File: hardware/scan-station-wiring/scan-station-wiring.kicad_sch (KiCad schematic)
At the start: 57 parts, among them J10 Buttons/Encoder, J11 GPIO Expansion, J1A CYD Expansion (SPI2), J1B CYD UART (PWR+HS), J2 NFC Antenna A, J3 RGB LED Header, J4 NFC Antenna B, J5 USB-C Power, J6 Load Cell, J7 CAN Bus, J8 I2C1 Expansion, J9 TOF Sensor (I2C1), Q1 TVDD_SW_A, Q2 TVDD_SW_B, Q3 BSS138 (SDA), Q4 BSS138 (SCL), U1 ESP32-S3-DevKitC-1, U2 ADS1220IPWR, U3 AHT20, U4 PN5180A0HN, U5 AS7341-DLGM, U6 AMS1117-3.3, U7 SN65HVD230DR, U8 AMS1117-1.8, Y1 27.12MHz

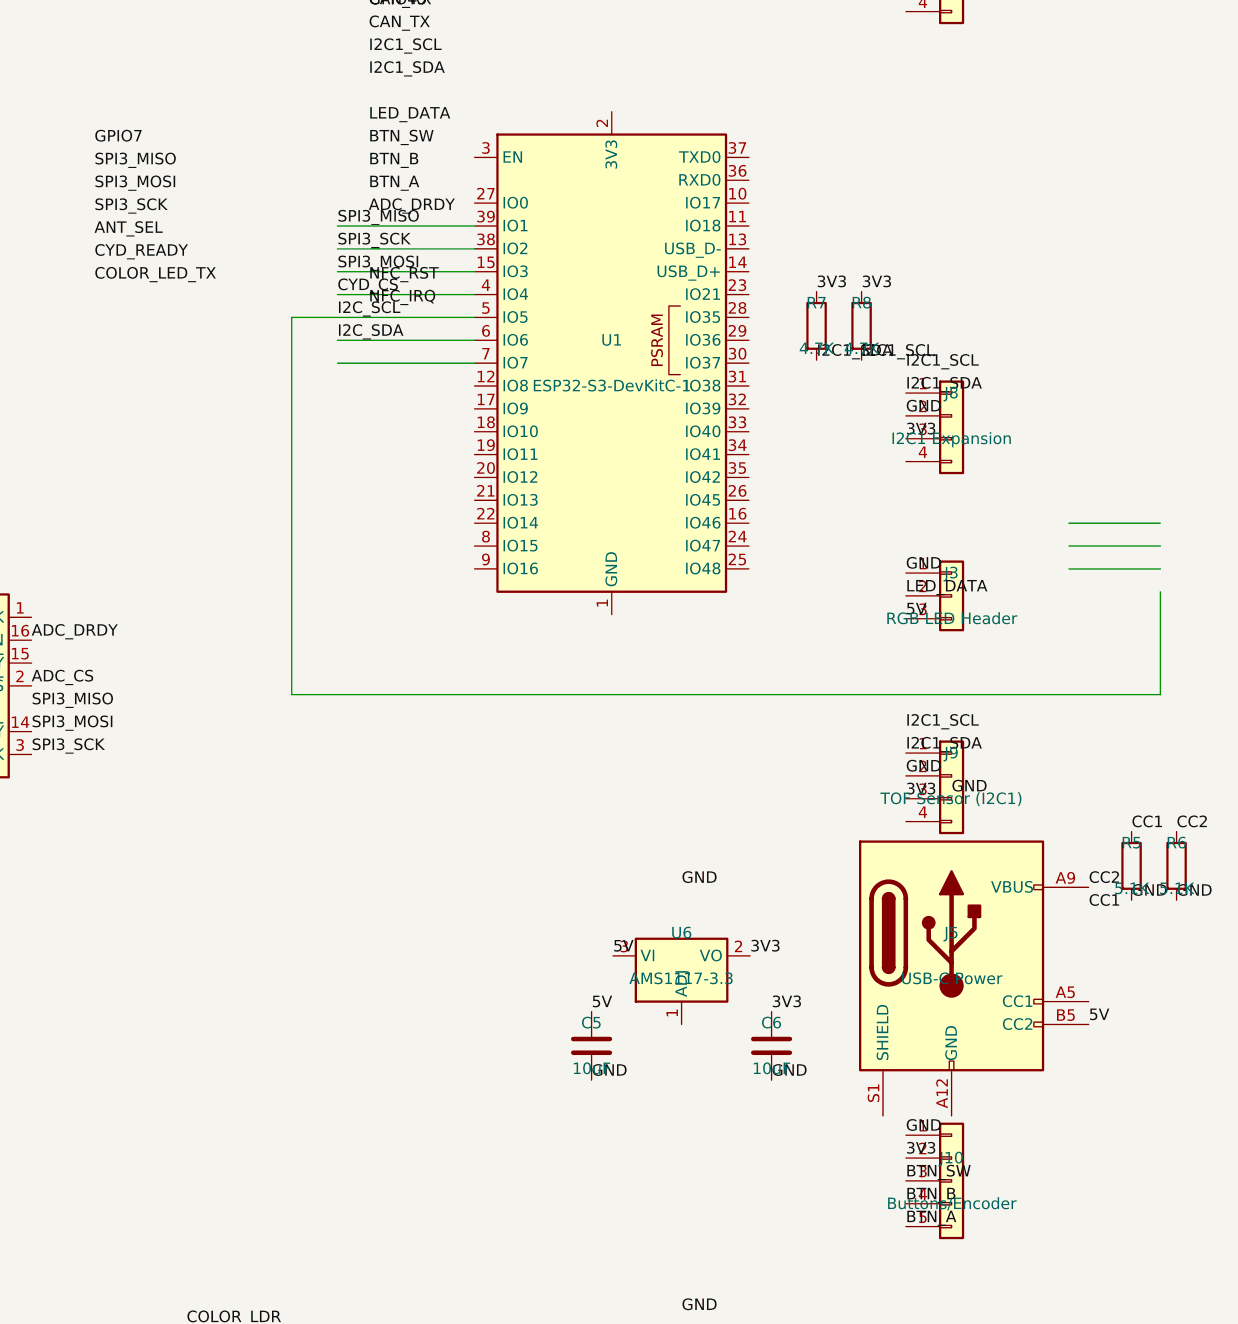
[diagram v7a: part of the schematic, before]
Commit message: feat: switch from DevKitC to bare ESP32-S3-WROOM-1 module
Eliminates redundant USB, regulator, and buttons from DevKitC.
Adds required support circuitry for bare module:

- EN circuit: 10K pull-up + 1uF cap + reset button (SW1)
- Boot button (SW2): GPIO0 + 10K pull-up
- Native USB: 22R series resistors on D+/D-, upgraded J5 to
  USB-C 2.0 14P receptacle (was power-only 6P)
- Module decoupling: 10uF + 100nF on 3V3 input
- Saves ~$5/board vs DevKitC, smaller PCB footprint

Co-Authored-By: Claude Opus 4.6 (1M context) <noreply@anthropic.com>
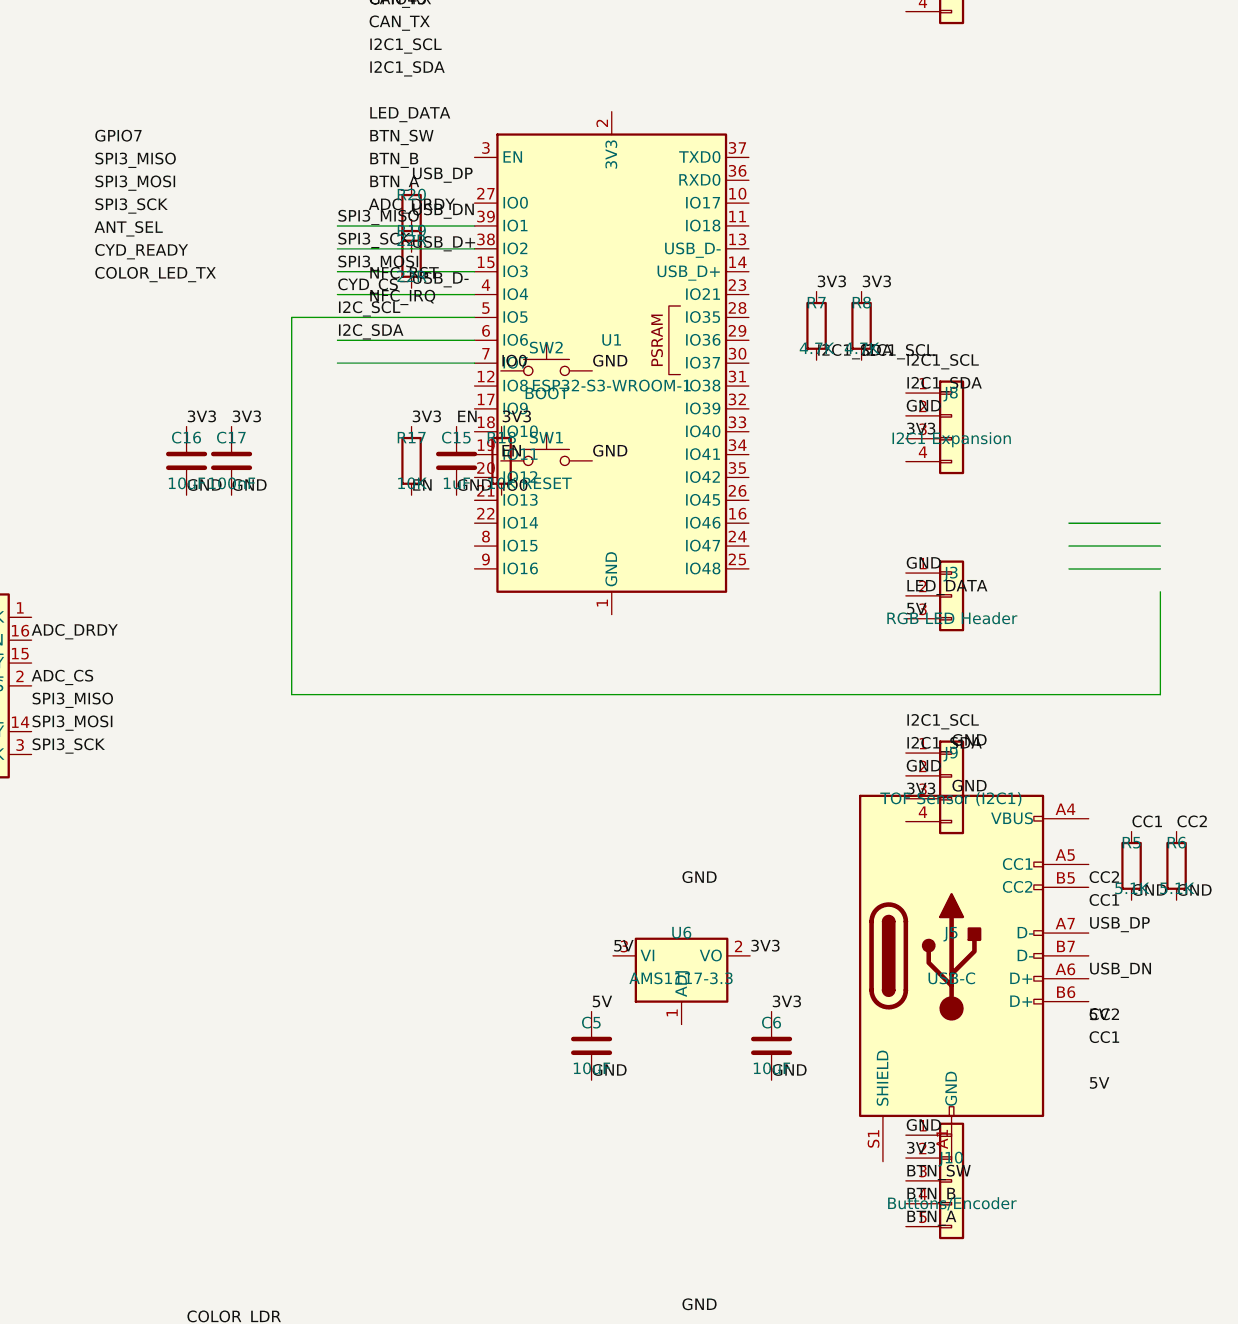
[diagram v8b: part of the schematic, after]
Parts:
- removed J5: USB-C Power, symbol Connector:USB_C_Receptacle_PowerOnly_6P
- added C15: 1uF, symbol Device:C
- added C16: 10uF, symbol Device:C
- added C17: 100nF, symbol Device:C
- added J5: USB-C, symbol Connector:USB_C_Receptacle_USB2.0_14P
- added R17, R18: 10K, symbol Device:R
- added R19, R20: 22R, symbol Device:R
- added SW1: RESET, symbol Switch:SW_Push
- added SW2: BOOT, symbol Switch:SW_Push
- U1: value ESP32-S3-DevKitC-1 -> ESP32-S3-WROOM-1
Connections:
- net CC2 is gone; now on net 5V: R6.1
- net 3V3: now also C16.1, C17.1, R17.1, R18.1
- net 5V: now also J5.B5 (CC2)
- net GND: now also C15.2, C16.2, C17.2, SW1.2, SW2.2
- new net: J5.A1 (GND), J5.A12 (GND), J5.B1 (GND), J5.B12 (GND)
- new net: J5.A4 (VBUS), J5.A9 (VBUS), J5.B4 (VBUS), J5.B9 (VBUS)
- new net EN: C15.1, R17.2, SW1.1
- new net IO0: R18.2, SW2.1
- new net USB_D+: R20.2
- new net USB_D-: R19.2
- new net USB_DN: J5.A6 (D+), R19.1
- new net USB_DP: J5.A7 (D-), R20.1
